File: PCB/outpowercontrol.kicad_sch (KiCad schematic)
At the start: 10 parts

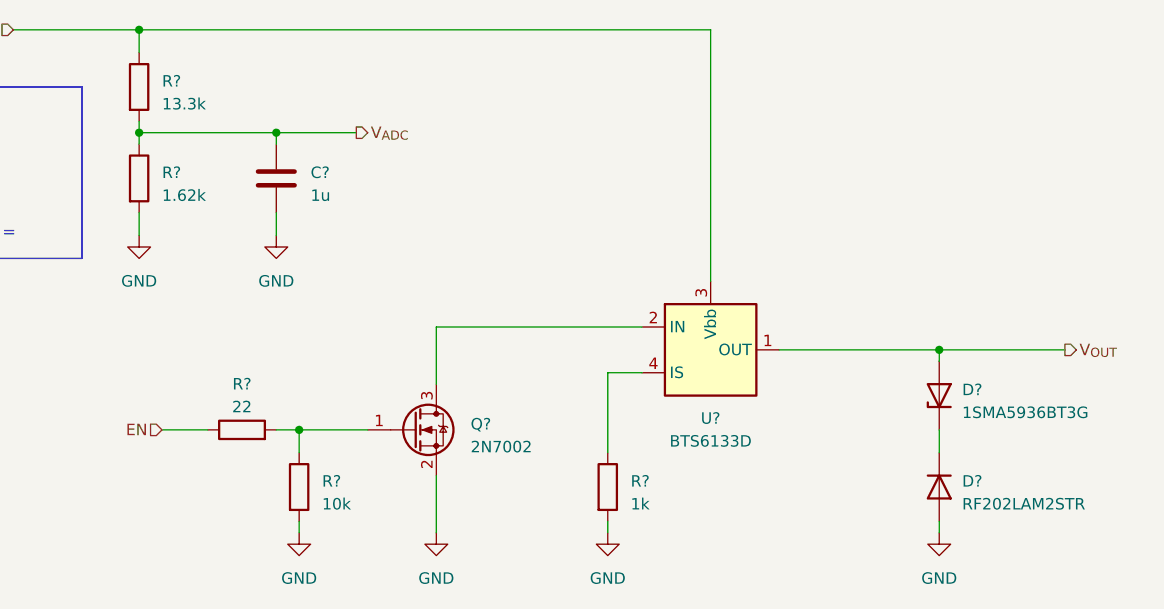
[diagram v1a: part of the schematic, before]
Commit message: done with sch before ERC and footprints
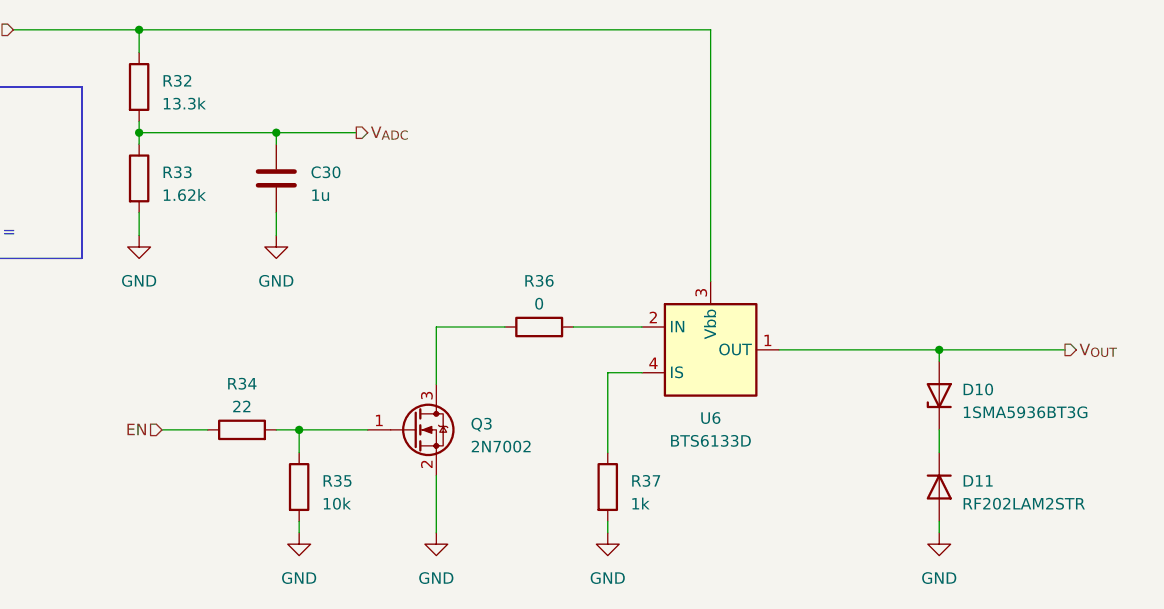
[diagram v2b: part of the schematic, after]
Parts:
- added R36: 0, symbol Device:R
- gave numbers to parts that had none: 10
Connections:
- net at Q3.3 (D): now also R36.1; no longer U6.2 (IN)
- new net: R36.2, U6.2 (IN)

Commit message: begin BOM
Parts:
- C30: footprint (none) -> Capacitor_SMD:C_0603_1608Metric; MPN (none) -> CGA3E1X7R1V105K080AC; Manufacturer (none) -> TDK
- D10: MPN (none) -> 1SMA5936BT3G; Manufacturer (none) -> Onsemi
- D11: MPN (none) -> RF202LAM2STR; Manufacturer (none) -> ROHM
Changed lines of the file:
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@@
       (effects (font (size 1.27 1.27)) (justify left) hide)
     )
+    (property "MPN" "" (at 132.08 118.11 0)
+      (effects (font (size 1.27 1.27)) hide)
+    )
+    (property "Manufacturer" "" (at 132.08 118.11 0)
+      (effects (font (size 1.27 1.27)) hide)
+    )
     (pin "1")
     (pin "2")
@@
       (effects (font (size 1.27 1.27)) hide)
     )
+    (property "MPN" "" (at 101.6 90.17 0)
+      (effects (font (size 1.27 1.27)) hide)
+    )
+    (property "Manufacturer" "" (at 101.6 90.17 0)
+      (effects (font (size 1.27 1.27)) hide)
+    )
     (pin "1")
     (pin "2")
@@
       (effects (font (size 1.27 1.27)) hide)
     )
+    (property "MPN" "" (at 119.38 124.46 0)
+      (effects (font (size 1.27 1.27)) hide)
+    )
+    (property "Manufacturer" "" (at 119.38 124.46 0)
+      (effects (font (size 1.27 1.27)) hide)
+    )
     (pin "1")
     (pin "2")
@@
       (effects (font (size 1.27 1.27)) (justify left))
     )
-    (property "Footprint" "" (at 117.8052 93.98 0)
+    (property "Footprint" "Capacitor_SMD:C_0603_1608Metric" (at 117.8052 93.98 0)
       (effects (font (size 1.27 1.27)) hide)
     )
@@
       (effects (font (size 1.27 1.27)) hide)
     )
+    (property "MPN" "CGA3E1X7R1V105K080AC" (at 116.84 90.17 0)
+      (effects (font (size 1.27 1.27)) hide)
+    )
+    (property "Manufacturer" "TDK" (at 116.84 90.17 0)
+      (effects (font (size 1.27 1.27)) hide)
+    )
     (pin "1")
     (pin "2")
@@
       (effects (font (size 1.27 1.27)) hide)
     )
+    (property "MPN" "" (at 101.6 80.01 0)
+      (effects (font (size 1.27 1.27)) hide)
+    )
+    (property "Manufacturer" "" (at 101.6 80.01 0)
+      (effects (font (size 1.27 1.27)) hide)
+    )
     (pin "1")
     (pin "2")
@@
     )
     (property "Datasheet" "http://www.infineon.com/dgdl/Infineon-BTS6133D-DS-v01_00-EN.pdf?fileId=5546d4625a888733015aa3e3286f102a" (at 165.1 119.38 0)
+      (effects (font (size 1.27 1.27)) hide)
+    )
+    (property "MPN" "" (at 165.1 109.22 0)
+      (effects (font (size 1.27 1.27)) hide)
+    )
+    (property "Manufacturer" "" (at 165.1 109.22 0)
       (effects (font (size 1.27 1.27)) hide)
     )
@@
     )
     (property "Datasheet" "~" (at 113.03 118.11 0)
+      (effects (font (size 1.27 1.27)) hide)
+    )
+    (property "MPN" "" (at 113.03 118.11 0)
+      (effects (font (size 1.27 1.27)) hide)
+    )
+    (property "Manufacturer" "" (at 113.03 118.11 0)
       (effects (font (size 1.27 1.27)) hide)
     )
@@
       (effects (font (size 1.27 1.27)) hide)
     )
+    (property "MPN" "1SMA5936BT3G" (at 190.5 114.3 0)
+      (effects (font (size 1.27 1.27)) hide)
+    )
+    (property "Manufacturer" "Onsemi" (at 190.5 114.3 0)
+      (effects (font (size 1.27 1.27)) hide)
+    )
     (pin "1")
     (pin "2")
@@
       (effects (font (size 1.27 1.27)) hide)
     )
+    (property "MPN" "" (at 153.67 124.46 0)
+      (effects (font (size 1.27 1.27)) hide)
+    )
+    (property "Manufacturer" "" (at 153.67 124.46 0)
+      (effects (font (size 1.27 1.27)) hide)
+    )
     (pin "1")
     (pin "2")
@@
       (effects (font (size 1.27 1.27)) hide)
     )
+    (property "MPN" "RF202LAM2STR" (at 190.5 124.46 0)
+      (effects (font (size 1.27 1.27)) hide)
+    )
+    (property "Manufacturer" "ROHM" (at 190.5 124.46 0)
+      (effects (font (size 1.27 1.27)) hide)
+    )
     (pin "1")
     (pin "2")
@@
       (effects (font (size 1.27 1.27)) hide)
     )
+    (property "MPN" "" (at 146.05 106.68 0)
+      (effects (font (size 1.27 1.27)) hide)
+    )
+    (property "Manufacturer" "" (at 146.05 106.68 0)
+      (effects (font (size 1.27 1.27)) hide)
+    )

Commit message: Resistors ok in BOM
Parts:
- Q3: MPN (none) -> 2N7002NXAKR; Manufacturer (none) -> Nexperia
- R32: footprint (none) -> Resistor_SMD:R_0603_1608Metric; MPN (none) -> ERJ-3EKF1332V; Manufacturer (none) -> Panasonic
- R33: footprint (none) -> Resistor_SMD:R_0603_1608Metric; MPN (none) -> ERJ-3EKF1621V; Manufacturer (none) -> Panasonic
- R34: footprint (none) -> Resistor_SMD:R_0603_1608Metric; MPN (none) -> ERJ-3EKF22R0V; Manufacturer (none) -> Panasonic
- R35: footprint (none) -> Resistor_SMD:R_0603_1608Metric; MPN (none) -> ERJ-3EKF1002V; Manufacturer (none) -> Panasonic
- R36: footprint (none) -> Resistor_SMD:R_0603_1608Metric; MPN (none) -> ERJ-3GEY0R00V; Manufacturer (none) -> Panasonic
- R37: footprint (none) -> Resistor_SMD:R_0603_1608Metric; MPN (none) -> ERJ-3EKF1001V; Manufacturer (none) -> Panasonic
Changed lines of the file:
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@@
       (effects (font (size 1.27 1.27)) (justify left) hide)
     )
-    (property "MPN" "" (at 132.08 118.11 0)
-      (effects (font (size 1.27 1.27)) hide)
-    )
-    (property "Manufacturer" "" (at 132.08 118.11 0)
+    (property "MPN" "2N7002NXAKR" (at 132.08 118.11 0)
+      (effects (font (size 1.27 1.27)) hide)
+    )
+    (property "Manufacturer" "Nexperia" (at 132.08 118.11 0)
       (effects (font (size 1.27 1.27)) hide)
     )
@@
       (effects (font (size 1.27 1.27)) (justify left))
     )
-    (property "Footprint" "" (at 99.822 90.17 90)
+    (property "Footprint" "Resistor_SMD:R_0603_1608Metric" (at 99.822 90.17 90)
       (effects (font (size 1.27 1.27)) hide)
     )
@@
       (effects (font (size 1.27 1.27)) hide)
     )
-    (property "MPN" "" (at 101.6 90.17 0)
-      (effects (font (size 1.27 1.27)) hide)
-    )
-    (property "Manufacturer" "" (at 101.6 90.17 0)
+    (property "MPN" "ERJ-3EKF1621V" (at 101.6 90.17 0)
+      (effects (font (size 1.27 1.27)) hide)
+    )
+    (property "Manufacturer" "Panasonic" (at 101.6 90.17 0)
       (effects (font (size 1.27 1.27)) hide)
     )
@@
       (effects (font (size 1.27 1.27)) (justify left))
     )
-    (property "Footprint" "" (at 117.602 124.46 90)
+    (property "Footprint" "Resistor_SMD:R_0603_1608Metric" (at 117.602 124.46 90)
       (effects (font (size 1.27 1.27)) hide)
     )
@@
       (effects (font (size 1.27 1.27)) hide)
     )
-    (property "MPN" "" (at 119.38 124.46 0)
-      (effects (font (size 1.27 1.27)) hide)
-    )
-    (property "Manufacturer" "" (at 119.38 124.46 0)
+    (property "MPN" "ERJ-3EKF1002V" (at 119.38 124.46 0)
+      (effects (font (size 1.27 1.27)) hide)
+    )
+    (property "Manufacturer" "Panasonic" (at 119.38 124.46 0)
       (effects (font (size 1.27 1.27)) hide)
     )
@@
       (effects (font (size 1.27 1.27)) (justify left))
     )
-    (property "Footprint" "" (at 99.822 80.01 90)
+    (property "Footprint" "Resistor_SMD:R_0603_1608Metric" (at 99.822 80.01 90)
       (effects (font (size 1.27 1.27)) hide)
     )
@@
       (effects (font (size 1.27 1.27)) hide)
     )
-    (property "MPN" "" (at 101.6 80.01 0)
-      (effects (font (size 1.27 1.27)) hide)
-    )
-    (property "Manufacturer" "" (at 101.6 80.01 0)
+    (property "MPN" "ERJ-3EKF1332V" (at 101.6 80.01 0)
+      (effects (font (size 1.27 1.27)) hide)
+    )
+    (property "Manufacturer" "Panasonic" (at 101.6 80.01 0)
       (effects (font (size 1.27 1.27)) hide)
     )
@@
       (effects (font (size 1.27 1.27)))
     )
-    (property "Footprint" "" (at 113.03 119.888 90)
+    (property "Footprint" "Resistor_SMD:R_0603_1608Metric" (at 113.03 119.888 90)
       (effects (font (size 1.27 1.27)) hide)
     )
@@
       (effects (font (size 1.27 1.27)) hide)
     )
-    (property "MPN" "" (at 113.03 118.11 0)
-      (effects (font (size 1.27 1.27)) hide)
-    )
-    (property "Manufacturer" "" (at 113.03 118.11 0)
+    (property "MPN" "ERJ-3EKF22R0V" (at 113.03 118.11 0)
+      (effects (font (size 1.27 1.27)) hide)
+    )
+    (property "Manufacturer" "Panasonic" (at 113.03 118.11 0)
       (effects (font (size 1.27 1.27)) hide)
     )
@@
       (effects (font (size 1.27 1.27)) (justify left))
     )
-    (property "Footprint" "" (at 151.892 124.46 90)
+    (property "Footprint" "Resistor_SMD:R_0603_1608Metric" (at 151.892 124.46 90)
       (effects (font (size 1.27 1.27)) hide)
     )
@@
       (effects (font (size 1.27 1.27)) hide)
     )
-    (property "MPN" "" (at 153.67 124.46 0)
-      (effects (font (size 1.27 1.27)) hide)
-    )
-    (property "Manufacturer" "" (at 153.67 124.46 0)
+    (property "MPN" "ERJ-3EKF1001V" (at 153.67 124.46 0)
+      (effects (font (size 1.27 1.27)) hide)
+    )
+    (property "Manufacturer" "Panasonic" (at 153.67 124.46 0)
       (effects (font (size 1.27 1.27)) hide)
     )
@@
       (effects (font (size 1.27 1.27)))
     )
-    (property "Footprint" "" (at 146.05 108.458 90)
+    (property "Footprint" "Resistor_SMD:R_0603_1608Metric" (at 146.05 108.458 90)
       (effects (font (size 1.27 1.27)) hide)
     )
@@
       (effects (font (size 1.27 1.27)) hide)
     )
-    (property "MPN" "" (at 146.05 106.68 0)
-      (effects (font (size 1.27 1.27)) hide)
-    )
-    (property "Manufacturer" "" (at 146.05 106.68 0)
-      (effects (font (size 1.27 1.27)) hide)
-    )
+    (property "MPN" "ERJ-3GEY0R00V" (at 146.05 106.68 0)
+      (effects (font (size 1.27 1.27)) hide)
+    )
+    (property "Manufacturer" "Panasonic" (at 146.05 106.68 0)
+      (effects (font (size 1.27 1.27)) hide)
+    )

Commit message: bom almost finished
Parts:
- U6: MPN (none) -> BTS6133D; Manufacturer (none) -> Infineon
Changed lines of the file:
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@@
       (effects (font (size 1.27 1.27)) hide)
     )
-    (property "MPN" "" (at 165.1 109.22 0)
+    (property "MPN" "BTS6133D" (at 165.1 109.22 0)
       (effects (font (size 1.27 1.27)) hide)
     )
-    (property "Manufacturer" "" (at 165.1 109.22 0)
+    (property "Manufacturer" "Infineon" (at 165.1 109.22 0)
       (effects (font (size 1.27 1.27)) hide)
     )
@@
       (effects (font (size 1.27 1.27)) hide)
     )
-    (property "Sim.Device" "D" (at 190.5 124.46 0)
-      (effects (font (size 1.27 1.27)) hide)
-    )
-    (property "Sim.Pins" "1=K 2=A" (at 190.5 124.46 0)
-      (effects (font (size 1.27 1.27)) hide)
-    )

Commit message: choose new power sw
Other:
- note added: "TPS25974ARPWR"
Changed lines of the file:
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@@
+		)
+	)
+	(text "TPS25974ARPWR"
+		(exclude_from_sim no)
+		(at 137.668 59.436 0)
+		(effects
+			(font
+				(size 1.27 1.27)
+			)
 		)
 	)

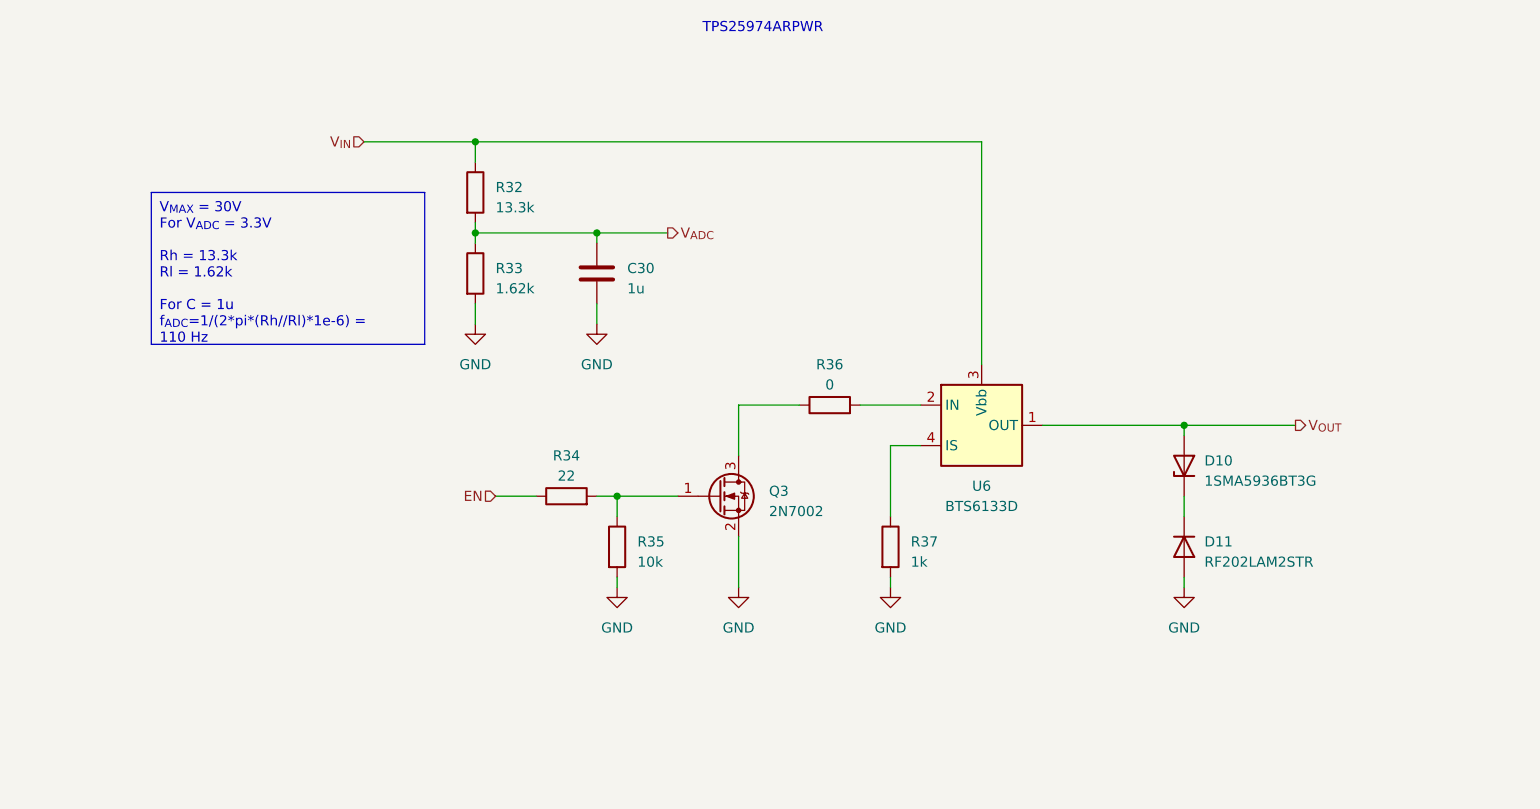
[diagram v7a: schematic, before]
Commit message: ok for efuse w/o values
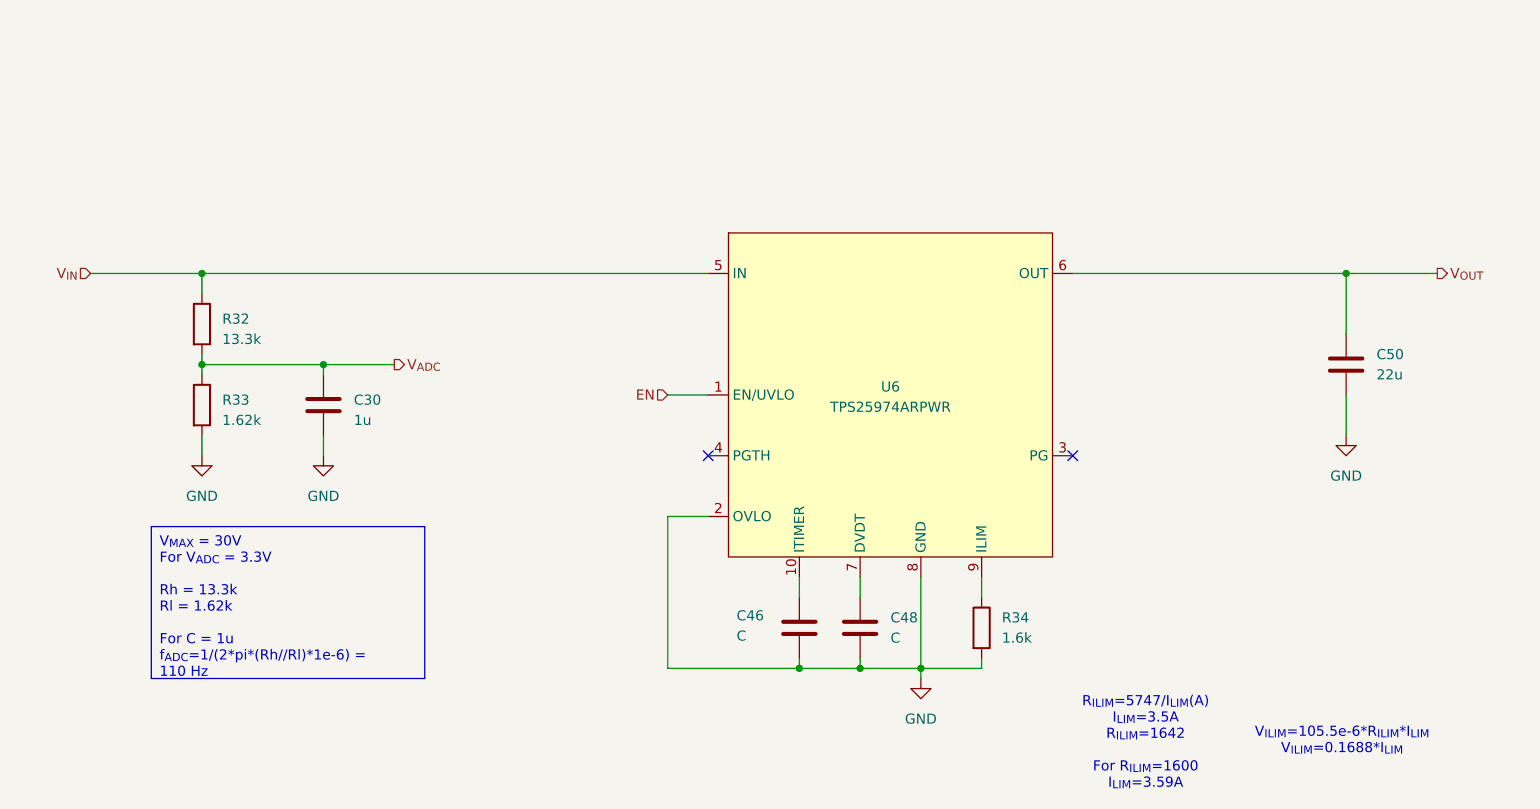
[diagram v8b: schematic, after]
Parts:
- removed D10: 1SMA5936BT3G, Diode_SMD:D_SMA, symbol Device:D_Zener
- removed D11: RF202LAM2STR, Diode_SMD:D_SOD-128, symbol Device:D
- removed Q3: 2N7002, Package_TO_SOT_SMD:SOT-23, symbol Transistor_FET:2N7002
- removed R35: 10k, Resistor_SMD:R_0603_1608Metric, symbol Device:R
- removed R36: 0, Resistor_SMD:R_0603_1608Metric, symbol Device:R
- removed R37: 1k, Resistor_SMD:R_0603_1608Metric, symbol Device:R
- removed U6: BTS6133D, Package_TO_SOT_SMD:TO-252-4, symbol Power_Management:BTS6133D
- added C46, C48: C, symbol Device:C
- added C50: 22u, symbol Device:C
- added U6: TPS25974ARPWR, TattooSupplyFootprints:TPS25947, symbol TattooSupplyLib:TPS25974x
- R34: value 22 -> 1.6k; footprint Resistor_SMD:R_0603_1608Metric -> (none); MPN ERJ-3EKF22R0V -> (none); Manufacturer Panasonic -> (none)
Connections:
- net EN: now also U6.1 (EN/UVLO); no longer R34.1
- net GND: now also R34.2, C46.2, C48.2, C50.2, U6.2 (OVLO), U6.8 (GND)
- net V_{IN}: now also U6.5 (IN)
- net V_{OUT}: now also C50.1, U6.6 (OUT)
- new net: C46.1, U6.10 (ITIMER)
- new net: C48.1, U6.7 (DVDT)
- new net: R34.1, U6.9 (ILIM)
- no-connect marks 0 -> 2
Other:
- note added: "R_{ILIM}=5747/I_{LIM}(A) I_{LIM}=3.5A R_{ILIM}=1642 For R_{ILIM}=1600 I_{LIM}=3.59A"
- note added: "V_{ILIM}=105.5e-6*R_{ILIM}*I_{LIM} V_{ILIM}=0.1688*I_{LIM}"
- note removed: "TPS25974ARPWR"
- moved on the sheet: C30, R32, R33
